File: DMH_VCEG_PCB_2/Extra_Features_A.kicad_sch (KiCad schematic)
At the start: 47 parts, among them J22 Conn_01x10_PinHeader, J23 Conn_01x10_PinHeader, Q4 BC548, SW1 SW_DPDT_x2, SW3 SW_SPDT_321_OnOff, SW4 SW_SPDT_321_OnOff, U1 TL074, U19 4001, U3 40106, U8 TL074

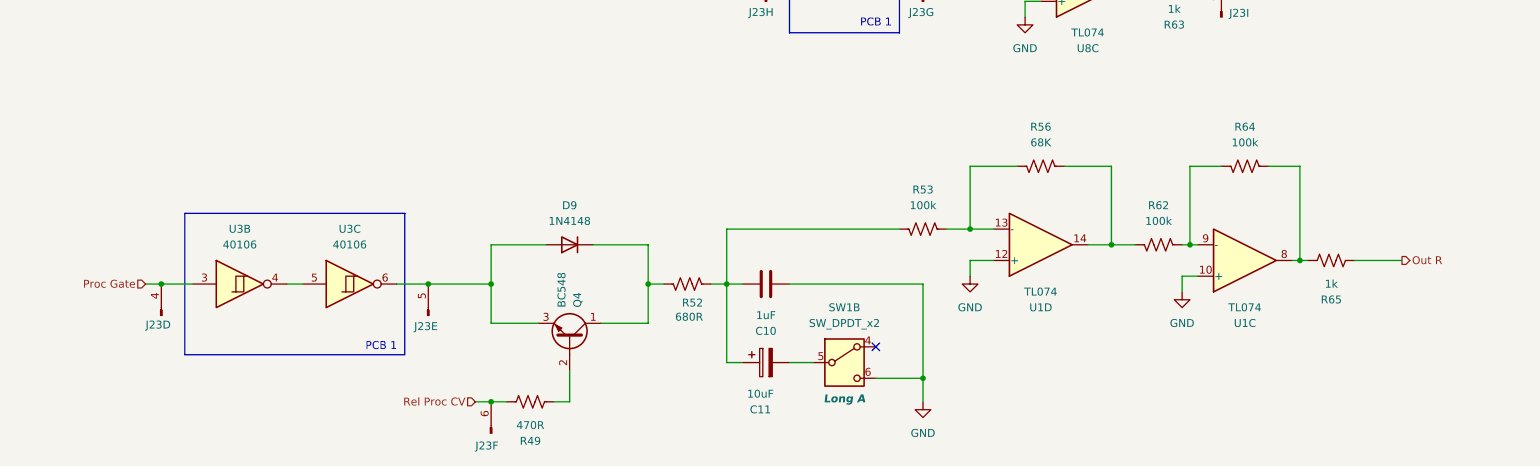
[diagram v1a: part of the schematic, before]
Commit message: Placed ICs and pin headers on PCB 2
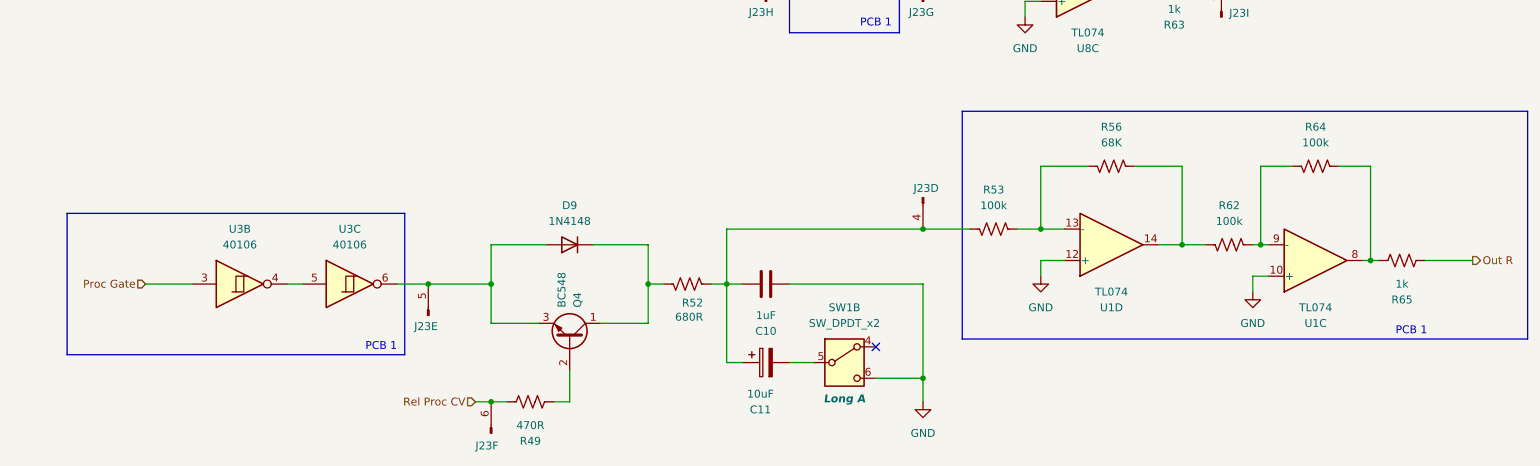
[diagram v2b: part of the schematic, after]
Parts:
- J22, J23: footprint (none) -> Connector_PinSocket_2.54mm:PinSocket_1x10_P2.54mm_Vertical
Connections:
- net Proc Gate: no longer J23.4 (Pin_4)
- net at C10.1, C11.1, R52.1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: now also J23.4 (Pin_4)
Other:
- moved on the sheet: R53, R56, R62, R64, R65, U1C, U1D

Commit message: Addition of manual gate ongoing
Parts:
- removed SW4: SW_SPDT_321_OnOff, SynthStuff:Toggle_Switch_TE, symbol SynthStuff:SW_SPDT_321_OnOff
- added C63: 100nF, Capacitor_THT:C_Disc_D4.3mm_W1.9mm_P5.00mm, symbol Device:C
- added D29: 1N4148, Diode_THT:D_DO-35_SOD27_P7.62mm_Horizontal, symbol Diode:1N4148
- added unit 2 of J23
- added R159: 10k, Resistor_THT:R_Axial_DIN0207_L6.3mm_D2.5mm_P7.62mm_Horizontal, symbol Device:R_US
- added R160: 47k, Resistor_THT:R_Axial_DIN0207_L6.3mm_D2.5mm_P7.62mm_Horizontal, symbol Device:R_US
- added SW4: SW_DPDT_x2_On-Off-(On), symbol Switch:SW_DPDT_x2
- added unit 5 of U3
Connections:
- net +12V: now also R160.1
- net GND: now also C63.2, SW4.4 (A)
- net Loop: now also SW4.3 (C)
- net Proc Gate: now also D29.1 (K)
- net at C59.2: now also SW4.2 (B)
- new net: R159.1, SW4.5 (B)
- new net: C63.1, J23.2 (Pin_2), R159.2, R160.2, U3.11
- new net: D29.2 (A), U3.10
- no-connect marks 3 -> 4

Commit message: Copied Manual Gate circuit to PCB 1 schematic
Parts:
- SW4: footprint (none) -> SynthStuff:Toggle_Switch_2_Poles_TE
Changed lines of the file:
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@@
 			)
 		)
-		(property "Footprint" ""
+		(property "Footprint" "SynthStuff:Toggle_Switch_2_Poles_TE"
 			(at 101.6 127 0)
 			(effects
@@
 			)
 		)
-		(property "Footprint" ""
+		(property "Footprint" "SynthStuff:Toggle_Switch_2_Poles_TE"
 			(at 109.22 22.86 0)
 			(effects

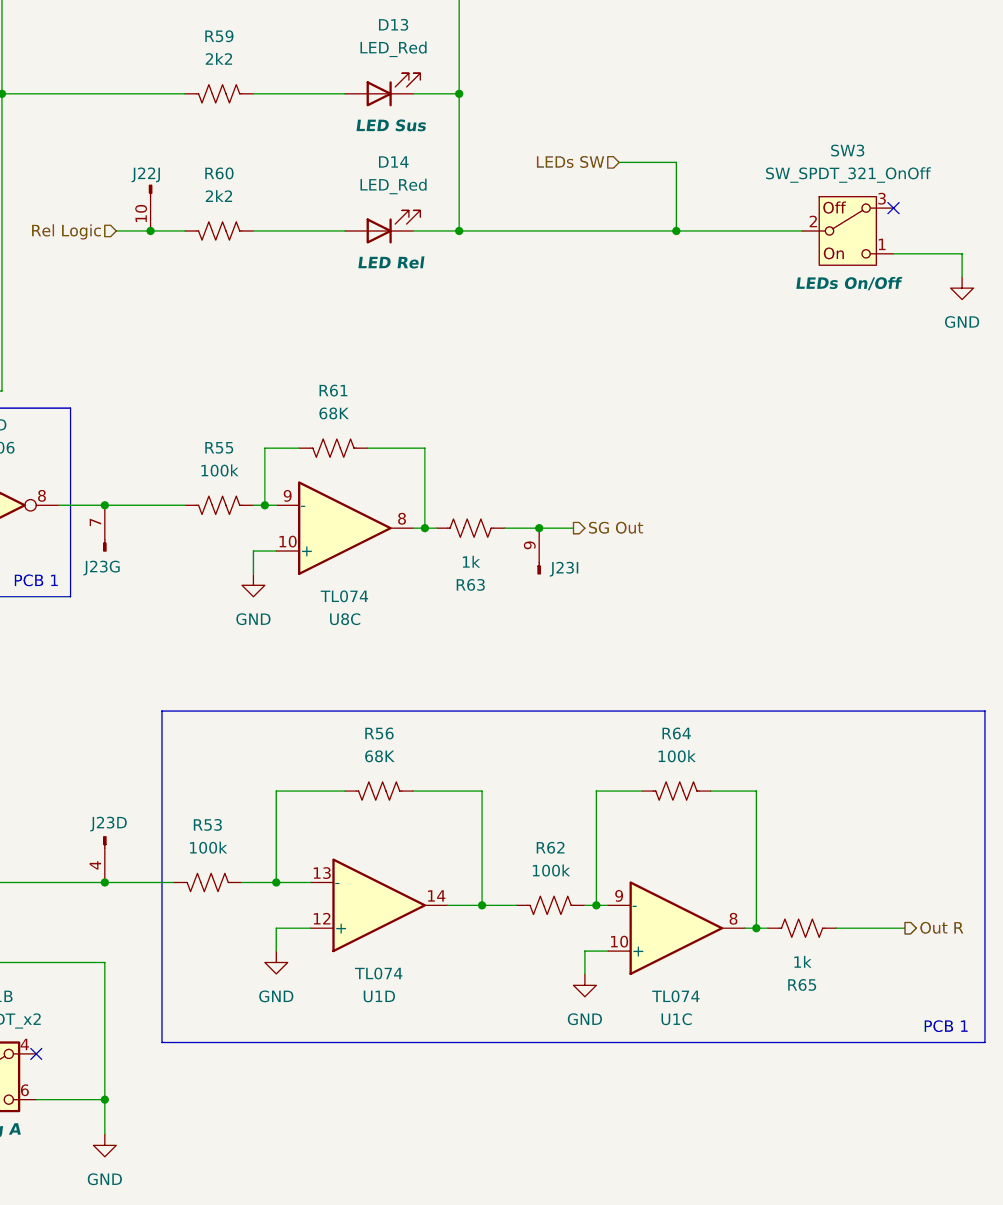
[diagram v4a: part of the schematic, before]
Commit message: Added Output attenuation circuit
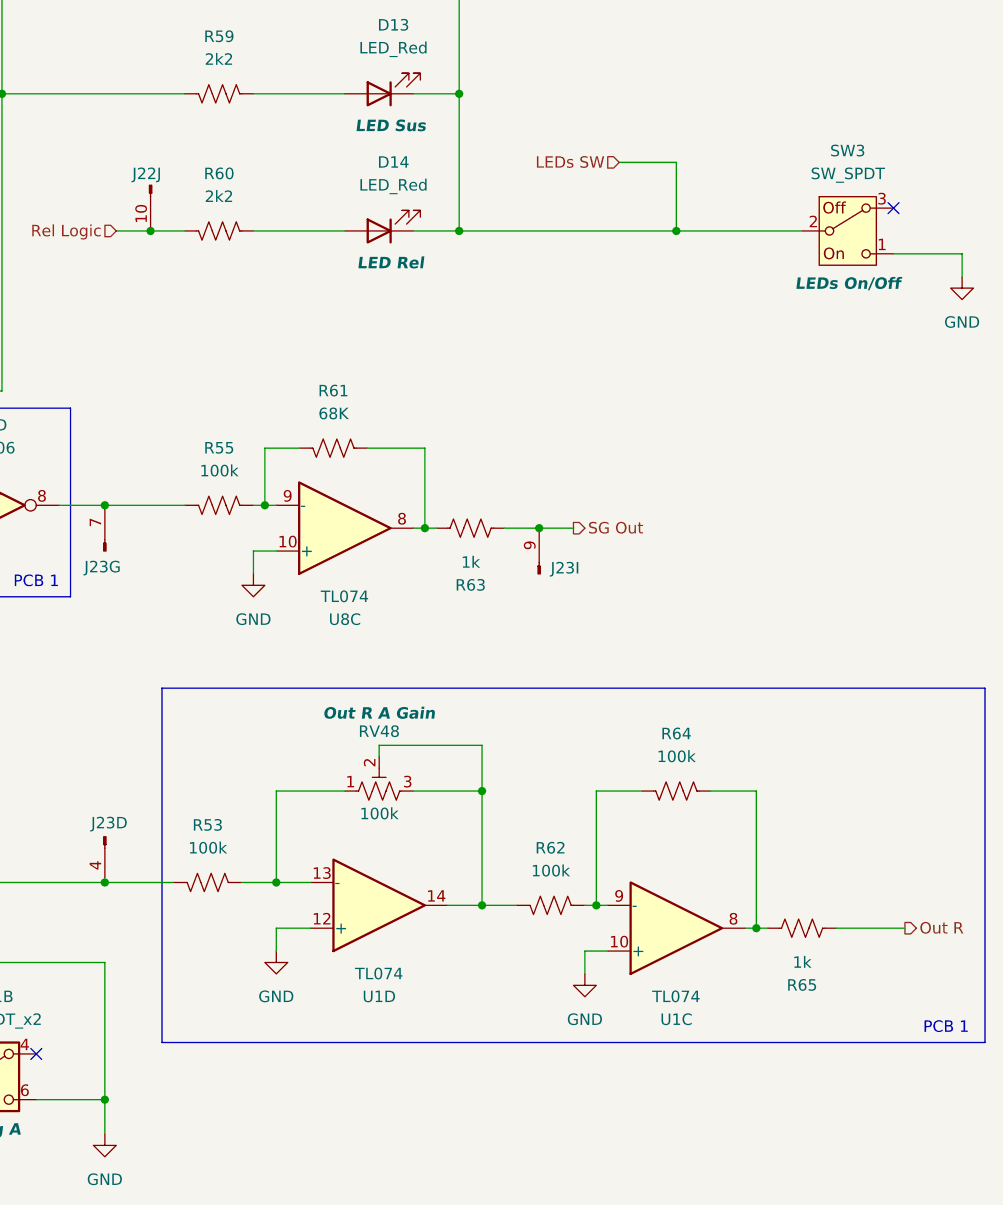
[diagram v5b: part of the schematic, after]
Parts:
- removed R56: 68K, Resistor_THT:R_Axial_DIN0207_L6.3mm_D2.5mm_P7.62mm_Horizontal, symbol Device:R_US
- added RV48: 100k, Potentiometer_THT:Potentiometer_Bourns_3296X_Horizontal, symbol Device:R_Potentiometer_Trim_US
- SW3: value SW_SPDT_321_OnOff -> SW_SPDT
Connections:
- net at R53.2, U1.13 (-): now also RV48.1
- net at R62.1, U1.14: now also RV48.2, RV48.3
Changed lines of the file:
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@@
 	)
 	(rectangle
-		(start 165.1 124.46)
+		(start 165.1 121.92)
 		(end 256.54 161.29)
 		(stroke
@@
 	)
 	(junction
+		(at 200.66 133.35)
+		(diameter 0)
+		(color 0 0 0 0)
+	)
+	(junction
 		(at 200.66 146.05)
 		(diameter 0)
@@
 	(wire
 		(pts
+			(xy 189.23 128.27) (xy 200.66 128.27)
+		)
+		(stroke
+			(width 0)
+			(type default)
+		)
+	)
+	(wire
+		(pts
 			(xy 177.8 143.51) (xy 173.99 143.51)
 		)
@@
 	(wire
 		(pts
+			(xy 189.23 129.54) (xy 189.23 128.27)
+		)
+		(stroke
+			(width 0)
+			(type default)
+		)
+	)
+	(wire
+		(pts
 			(xy 101.6 50.8) (xy 106.68 50.8)
 		)
@@
 	(wire
 		(pts
+			(xy 200.66 128.27) (xy 200.66 133.35)
+		)
+		(stroke
+			(width 0)
+			(type default)
+		)
+	)
+	(wire
+		(pts
 			(xy 43.18 57.15) (xy 40.64 57.15)
 		)
@@
 			)
 		)
-		(property "Value" "SW_SPDT_321_OnOff"
+		(property "Value" "SW_SPDT"
 			(at 241.3 64.77 0)
 			(effects
@@
 	)
 	(symbol
+		(lib_id "Device:R_Potentiometer_Trim_US")
+		(at 189.23 133.35 90)
+		(unit 1)
+		(exclude_from_sim no)
+		(in_bom yes)
+		(on_board no)
+		(dnp no)
+		(property "Reference" "RV48"
+			(at 189.23 126.746 90)
+			(effects
+				(font
+					(size 1.27 1.27)
+				)
+			)
+		)
+		(property "Value" "100k"
+			(at 189.23 135.89 90)
+			(effects
+				(font
+					(size 1.27 1.27)
+				)
+			)
+		)
+		(property "Footprint" "Potentiometer_THT:Potentiometer_Bourns_3296X_Horizontal"
+			(at 189.23 133.35 0)
+			(effects
+				(font
+					(size 1.27 1.27)
+				)
+				(hide yes)
+			)
+		)
+		(property "Datasheet" "~"
+			(at 189.23 133.35 0)
+			(effects
+				(font
+					(size 1.27 1.27)
+				)
+				(hide yes)
+			)
+		)
+		(property "Description" "Trim-potentiometer, US symbol"
+			(at 189.23 133.35 0)
+			(effects
+				(font
+					(size 1.27 1.27)
+				)
+				(hide yes)
+			)
+		)
+		(property "Function" "Out R A Gain"
+			(at 189.23 124.714 90)
+			(effects
+				(font
+					(size 1.27 1.27)
+					(thickness 0.254)
+					(bold yes)
+					(italic yes)
+				)
+			)
+		)
+		(pin "2"
+		)
+		(pin "1"
+		)
+		(pin "3"
+		)
+		(instances
+			(project "DMH_VCEG_PCB_2"
+				(path "/58f4306d-5387-4983-bb08-41a2313fd315/dfc6a801-157b-43f6-bf92-8048d56e52a2"
+					(reference "RV48")
+					(unit 1)
+				)
+			)
+		)
+	)
+	(symbol
 		(lib_id "power:+12V")
 		(at 82.55 113.03 0)
@@
 				)
 			)
-		)
-	)
-	(symbol
-		(lib_id "Device:R_US")
-		(at 189.23 133.35 90)
-		(mirror x)
-		(unit 1)
-		(exclude_from_sim no)
-		(in_bom yes)
-		(on_board no)
-		(dnp no)
-		(property "Reference" "R56"
-			(at 189.23 127 90)
-			(effects
-				(font
-					(size 1.27 1.27)
-				)
-			)
-		)
-		(property "Value" "68K"
-			(at 189.23 129.54 90)
-			(effects
-				(font
-					(size 1.27 1.27)
-				)
-			)
-		)
-		(property "Footprint" "Resistor_THT:R_Axial_DIN0207_L6.3mm_D2.5mm_P7.62mm_Horizontal"
-			(at 189.484 134.366 90)
-			(effects
-				(font
-					(size 1.27 1.27)
-				)
-				(hide yes)
-			)
-		)
-		(property "Datasheet" "~"
-			(at 189.23 133.35 0)
-			(effects
-				(font
-					(size 1.27 1.27)
-				)
-				(hide yes)
-			)
-		)
-		(property "Description" "Resistor, US symbol"
-			(at 189.23 133.35 0)
-			(effects
-				(font
-					(size 1.27 1.27)
-				)
-				(hide yes)
-			)
-		)
-		(pin "2"
-		)
-		(pin "1"
-		)
-		(instances
-			(project "DMH_VCEG_PCB_1"
-				(path "/58f4306d-5387-4983-bb08-41a2313fd315/dfc6a801-157b-43f6-bf92-8048d56e52a2"
-					(reference "R56")
-					(unit 1)
-				)
-			)

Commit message: Synced PCB 2 project with PCB 1
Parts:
- removed C10: 1uF, Capacitor_THT:C_Disc_D4.3mm_W1.9mm_P5.00mm, symbol Device:C
- removed C11: 10uF, Capacitor_THT:CP_Radial_D5.0mm_P2.00mm, symbol Device:C_Polarized
- removed C55, C59: 1nF, Capacitor_THT:C_Disc_D4.3mm_W1.9mm_P5.00mm, symbol Device:C
- removed C63: 100nF, Capacitor_THT:C_Disc_D4.3mm_W1.9mm_P5.00mm, symbol Device:C
- removed D10, D27, D29, D9: 1N4148, Diode_THT:D_DO-35_SOD27_P7.62mm_Horizontal, symbol Diode:1N4148
- removed D11, D12, D13, D14: LED_Red, LED_THT:LED_D3.0mm, symbol Device:LED
- removed J22, J23: Conn_01x10_PinHeader, Connector_PinSocket_2.54mm:PinSocket_1x10_P2.54mm_Vertical, symbol SynthStuff:Conn_01x10_PinHeader
- removed Q4: BC548, Package_TO_SOT_THT:TO-92L_Inline_Wide, symbol Transistor_BJT:BC548
- removed R149, R154, R159: 10k, Resistor_THT:R_Axial_DIN0207_L6.3mm_D2.5mm_P7.62mm_Horizontal, symbol Device:R_US
- removed R150, R151, R152, R153, R45, R46, R47, R48, R53, R55, R62, R64: 100k, Resistor_THT:R_Axial_DIN0207_L6.3mm_D2.5mm_P7.62mm_Horizontal, symbol Device:R_US
- removed R160, R50: 47k, Resistor_THT:R_Axial_DIN0207_L6.3mm_D2.5mm_P7.62mm_Horizontal, symbol Device:R_US
- removed R49: 470R, Resistor_THT:R_Axial_DIN0207_L6.3mm_D2.5mm_P7.62mm_Horizontal, symbol Device:R_US
- removed R51: 100R, Resistor_THT:R_Axial_DIN0207_L6.3mm_D2.5mm_P7.62mm_Horizontal, symbol Device:R_US
- removed R52: 680R, Resistor_THT:R_Axial_DIN0207_L6.3mm_D2.5mm_P7.62mm_Horizontal, symbol Device:R_US
- removed R57, R58, R59, R60: 2k2, Resistor_THT:R_Axial_DIN0207_L6.3mm_D2.5mm_P7.62mm_Horizontal, symbol Device:R_US
- removed R61: 68K, Resistor_THT:R_Axial_DIN0207_L6.3mm_D2.5mm_P7.62mm_Horizontal, symbol Device:R_US
- removed R63, R65: 1k, Resistor_THT:R_Axial_DIN0207_L6.3mm_D2.5mm_P7.62mm_Horizontal, symbol Device:R_US
- removed RV48: 100k, Potentiometer_THT:Potentiometer_Bourns_3296X_Horizontal, symbol Device:R_Potentiometer_Trim_US
- removed SW1: SW_DPDT_x2, SynthStuff:Toggle_Switch_2_Poles_TE, symbol Switch:SW_DPDT_x2
- removed SW3: SW_SPDT, SynthStuff:Toggle_Switch_TE, symbol SynthStuff:SW_SPDT_321_OnOff
- removed SW4: SW_DPDT_x2_On-Off-(On), SynthStuff:Toggle_Switch_2_Poles_TE, symbol Switch:SW_DPDT_x2
- removed U1, U8: TL074, Package_DIP:DIP-14_W7.62mm_Socket, symbol Amplifier_Operational:TL074
- removed U19: 4001, Package_DIP:DIP-14_W7.62mm_Socket, symbol 4xxx:4001
- removed U3: 40106, Package_DIP:DIP-14_W7.62mm_Socket, symbol 4xxx:40106
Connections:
- no-connect marks 4 -> 0
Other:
- note removed: "PCB 1"
